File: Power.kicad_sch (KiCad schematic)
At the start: 3 parts, among them U3 MIC5365-3.3YD5

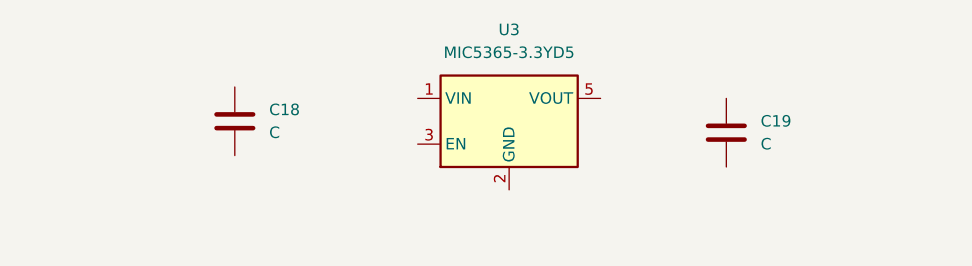
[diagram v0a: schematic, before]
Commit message: fixed some nets
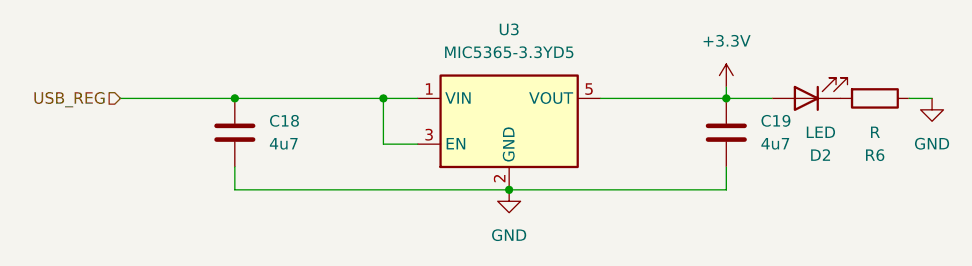
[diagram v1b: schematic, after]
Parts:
- added D2: LED, LED_SMD:LED_0402_1005Metric, symbol Device:LED
- added R6: R, Resistor_SMD:R_0402_1005Metric, symbol Device:R
- C18, C19: value C -> 4u7; footprint (none) -> Capacitor_SMD:C_0603_1608Metric
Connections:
- net USB_REG: now reaches U3.1 (VIN)
- net USB_REG: now also C18.1, U3.3 (EN)
- net GND: now reaches U3.2 (GND)
- net GND: now also C18.2, C19.2, R6.1
- net +3.3V: now reaches U3.5 (VOUT)
- net +3.3V: now also C19.1, D2.2 (A)
- new net: D2.1 (K), R6.2
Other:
- moved on the sheet: C18

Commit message: fixed drc error
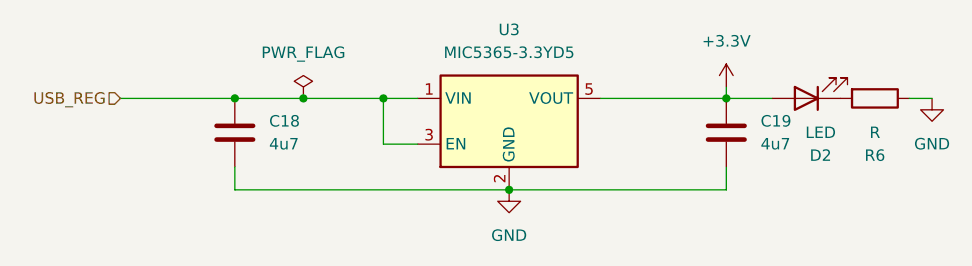
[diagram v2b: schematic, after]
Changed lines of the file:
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@@
 		(color 0 0 0 0)
 	)
+	(junction
+		(at 120.65 100.33)
+		(diameter 0)
+		(color 0 0 0 0)
+	)
 	(wire
 		(pts
@@
 	(wire
 		(pts
-			(xy 113.03 100.33) (xy 129.54 100.33)
+			(xy 113.03 100.33) (xy 120.65 100.33)
 		)
 		(stroke
@@
 		(pts
 			(xy 129.54 105.41) (xy 129.54 100.33)
+		)
+		(stroke
+			(width 0)
+			(type default)
+		)
+	)
+	(wire
+		(pts
+			(xy 120.65 100.33) (xy 129.54 100.33)
 		)
 		(stroke
@@
 					(unit 1)
 				)
+			)
+		)
+	)
+	(symbol
+		(lib_id "power:PWR_FLAG")
+		(at 120.65 100.33 0)
+		(unit 1)
+		(exclude_from_sim no)
+		(in_bom yes)
+		(on_board yes)
+		(dnp no)
+		(fields_autoplaced yes)
+		(property "Reference" "#FLG03"
+			(at 120.65 98.425 0)
+			(effects
+				(font
+					(size 1.27 1.27)
+				)
+				(hide yes)
+			)
+		)
+		(property "Value" "PWR_FLAG"
+			(at 120.65 95.25 0)
+			(effects
+				(font
+					(size 1.27 1.27)
+				)
+			)
+		)
+		(property "Footprint" ""
+			(at 120.65 100.33 0)
+			(effects
+				(font
+					(size 1.27 1.27)
+				)
+				(hide yes)
+			)
+		)
+		(property "Datasheet" "~"
+			(at 120.65 100.33 0)
+			(effects
+				(font
+					(size 1.27 1.27)
+				)
+				(hide yes)
+			)
+		)
+		(property "Description" "Special symbol for telling ERC where power comes from"
+			(at 120.65 100.33 0)
+			(effects
+				(font
+					(size 1.27 1.27)
+				)
+				(hide yes)
+			)
+		)
+		(pin "1"
+		)
+		(instances
+			(project "STM32 Bluetooth Hardware Design"
+				(path "/7294b0c1-22f8-4dfa-8bae-2337522835ff/fda3b057-34ad-441e-a643-0664d6ad0840"
+					(reference "#FLG03")
+					(unit 1)
+				)
